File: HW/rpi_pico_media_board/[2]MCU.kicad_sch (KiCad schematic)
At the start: 1 part

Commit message: Scheme improvements
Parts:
- added D200: PMEG1030EJ,115, Diode_SMD:D_SOD-323F, symbol Device:D_Schottky
- added D201, D202, D203, D204, D205, D206: PESD3V3L1BA,115, Diode_SMD:D_SOD-323, symbol Device:D_TVS
- added J200, J201: Conn_01x04_Pin, Connector_PinSocket_2.54mm:PinSocket_1x04_P2.54mm_Vertical, symbol Connector:Conn_01x04_Pin
- added SW200: SW_DPDT_XLX, rpi_pico_media_board:SW_DPDT_XLX, symbol rpi_pico_media_board:SW_DPDT_XLX
- added U202, U203: mems-mic, rpi_pico_media_board:inmp441, symbol rpi_pico_media_board:mems-mic
- renumbered A1 to U200
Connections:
- net UART0_TX: now reaches U200.1 (GPIO0)
- net UART0_TX: now also D203.1 (A1), J200.2 (Pin_2)
- net PCF8563_INT: now reaches U200.10 (GPIO7)
- net SPI1_SD_CARD_MISO: now reaches U200.11 (GPIO8)
- net SPI1_SD_CARD_CS: now reaches U200.12 (GPIO9)
- net GND: now reaches U200.13 (GND), U200.18 (GND), U200.23 (GND), U200.28 (GND), U200.3 (GND), U200.38 (GND), U200.8 (GND)
- net GND: now also D201.2 (A2), D202.2 (A2), D203.2 (A2), D204.2 (A2), D205.2 (A2), D206.2 (A2), J200.1 (Pin_1), J201.1 (Pin_1), U202.2 (GND), U203.2 (GND), U203.6 (SEL)
- net SPI1_SD_CARD_SCK: now reaches U200.14 (GPIO10)
- net SPI1_SD_CARD_MOSI: now reaches U200.15 (GPIO11)
- net SPI1_SD_CARD_CARD_DETECT: now reaches U200.16 (GPIO12)
- net I2S_INMP441_DATA: now reaches U200.17 (GPIO13)
- net I2S_INMP441_DATA: now also U202.4 (DOUT), U203.4 (DOUT)
- net I2S_INMP441_SCK: now reaches U200.19 (GPIO14)
- net I2S_INMP441_SCK: now also U202.3 (BCLK), U203.3 (BCLK)
- net UART0_RX: now reaches U200.2 (GPIO1)
- net UART0_RX: now also D202.1 (A1), J200.3 (Pin_3)
- net I2S_INMP441_SCL: now reaches U200.20 (GPIO15)
- net I2S_INMP441_SCL: now also U202.5 (LRCLK), U203.5 (LRCLK)
- net MACRO_PAD_BTN_COL_0: now reaches U200.21 (GPIO16)
- net MACRO_PAD_BTN_COL_1: now reaches U200.22 (GPIO17)
- net MACRO_PAD_BTN_COL_2: now reaches U200.24 (GPIO18)
- net MACRO_PAD_BTN_COL_3: now reaches U200.25 (GPIO19)
- net MACRO_PAD_BTN_ROW_0: now reaches U200.26 (GPIO20)
- net MACRO_PAD_BTN_ROW_1: now reaches U200.27 (GPIO21)
- net MACRO_PAD_BTN_ROW_2: now reaches U200.29 (GPIO22)
- net USR_LED_0: now reaches U200.31 (GPIO26_ADC0)
- net USR_LED_1: now reaches U200.32 (GPIO27_ADC1)
- net USR_LED_2: now reaches U200.34 (GPIO28_ADC2)
- net I2C1_SDA: now reaches U200.4 (GPIO2)
- net I2C1_SDA: now also D206.1 (A1), J201.2 (Pin_2)
- net +RPI_VBUS: now reaches U200.40 (VBUS)
- net +RPI_VBUS: now also SW200.2, SW200.5
- net I2C1_SCL: now reaches U200.5 (GPIO3)
- net I2C1_SCL: now also D205.1 (A1), J201.3 (Pin_3)
- net I2S_PCM5102_DATA: now reaches U200.6 (GPIO4)
- net I2S_PCM5102_SCK: now reaches U200.7 (GPIO5)
- net I2S_PCM5102_SCL: now reaches U200.9 (GPIO6)
- new net: D200.2 (A), SW200.3, SW200.4
- new net +3.3V: D201.1 (A1), D204.1 (A1), J200.4 (Pin_4), J201.4 (Pin_4)
- new net +3.3VA: U202.1 (3V), U202.6 (SEL), U203.1 (3V)
- new net VCC: D200.1 (K)
- no-connect marks 0 -> 8
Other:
- note added: "I2C1 PIN header"
- note added: "INM441 Microphone"
- note added: "UART PIN header"
- note added: "[2]MCU"
- moved on the sheet: U200

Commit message: Minor BOM updates
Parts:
- D200: Manufacturer (none) -> Nexperia; Manufacturer Part Number (none) -> PMEG1030EJ,115; Manufacturer_Name Nexperia -> (none); Manufacturer_Part_Number PMEG1030EJ,115 -> (none)
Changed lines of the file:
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@@
 			)
 		)
-		(property "Manufacturer_Name" "Nexperia"
+		(property "Manufacturer_Name" ""
 			(at 201.93 31.75 0)
 			(effects
@@
 			)
 		)
-		(property "Manufacturer_Part_Number" "PMEG1030EJ,115"
+		(property "Manufacturer_Part_Number" ""
 			(at 201.93 31.75 0)
 			(effects
+				(font
+					(size 1.27 1.27)
+				)
+				(hide yes)
+			)
+		)
+		(property "Manufacturer" "Nexperia"
+			(at 201.93 31.75 0)
+			(effects
+				(font
+					(size 1.27 1.27)
+				)
+				(hide yes)
+			)
+		)
+		(property "Manufacturer Part Number" "PMEG1030EJ,115"
+			(at 201.93 31.75 0)
+			(effects

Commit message: DRC cleanup
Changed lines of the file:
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@@
 	)
 	(global_label "I2S_INMP441_DATA"
-		(shape input)
+		(shape output)
 		(at 125.73 105.41 180)
 		(fields_autoplaced yes)
@@
 	)
 	(global_label "I2S_INMP441_DATA"
-		(shape input)
+		(shape output)
 		(at 80.01 149.86 0)
 		(fields_autoplaced yes)
@@
 		)
 	)
-	(global_label "I2S_INMP441_DATA"
-		(shape input)
-		(at 78.74 179.07 0)
-		(fields_autoplaced yes)
-		(effects
-			(font
-				(size 1.27 1.27)
-			)
-			(justify left)
-		)
-		(property "Intersheetrefs" "${INTERSHEET_REFS}"
-			(at 99.3842 179.07 0)
-			(effects
-				(font
-					(size 1.27 1.27)
-				)
-				(justify left)
-				(hide yes)
-			)
-		)
-	)
 	(global_label "MACRO_PAD_BTN_COL_2"
 		(shape input)
@@
 			(effects
 				(font
+					(size 1.27 1.27)
+				)
+				(justify left)
+				(hide yes)
+			)
+		)
+	)
+	(global_label "I2S_INMP441_DATA"
+		(shape output)
+		(at 78.74 179.07 0)
+		(fields_autoplaced yes)
+		(effects
+			(font
+				(size 1.27 1.27)
+			)
+			(justify left)
+		)
+		(property "Intersheetrefs" "${INTERSHEET_REFS}"
+			(at 99.3842 179.07 0)
+			(effects
+				(font

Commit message: PCB initial placement
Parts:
- U200: footprint Module_RaspberryPi_Pico:RaspberryPi_Pico_Common -> Module_RaspberryPi_Pico:RaspberryPi_Pico_Common_THT
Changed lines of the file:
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@@
 			)
 		)
-		(property "Footprint" "Module_RaspberryPi_Pico:RaspberryPi_Pico_Common"
+		(property "Footprint" "Module_RaspberryPi_Pico:RaspberryPi_Pico_Common_THT"
 			(at 153.67 144.78 0)
 			(effects

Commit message: Very initial PCB layout
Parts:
- removed D204: PESD3V3L1BA,115, Diode_SMD:D_SOD-323, symbol Device:D_TVS
- removed J201: Conn_01x04_Pin, Connector_PinSocket_2.54mm:PinSocket_1x04_P2.54mm_Vertical, symbol Connector:Conn_01x04_Pin
- added J201: Conn_01x03, Connector_PinSocket_2.54mm:PinSocket_1x03_P2.54mm_Vertical, symbol Connector_Generic:Conn_01x03
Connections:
- net GND: now also J201.1 (Pin_1)
- net I2C1_SCL: now also J201.3 (Pin_3)
- net I2C1_SDA: now also J201.2 (Pin_2)
- net +3.3VA renamed +3.3VA_INMP

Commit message: Macro Pad routing
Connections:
- net MACRO_PAD_BTN_ROW_0: now also U200.29 (GPIO22); no longer U200.26 (GPIO20)
- net MACRO_PAD_BTN_ROW_2: now also U200.26 (GPIO20); no longer U200.29 (GPIO22)
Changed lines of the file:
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@@
+	(wire
+		(pts
+			(xy 176.53 92.71) (xy 182.88 92.71)
+		)
+		(stroke
+			(width 0)
+			(type default)
+		)
+	)
 	(wire
 		(pts
@@
 	(wire
 		(pts
+			(xy 176.53 90.17) (xy 182.88 90.17)
+		)
+		(stroke
+			(width 0)
+			(type default)
+		)
+	)
+	(wire
+		(pts
 			(xy 125.73 82.55) (xy 130.81 82.55)
 		)
@@
 	(wire
 		(pts
+			(xy 176.53 95.25) (xy 182.88 95.25)
+		)
+		(stroke
+			(width 0)
+			(type default)
+		)
+	)
+	(wire
+		(pts
 			(xy 250.19 135.89) (xy 242.57 135.89)
 		)
@@
 	(wire
 		(pts
-			(xy 176.53 90.17) (xy 182.88 90.17)
-		)
-		(stroke
-			(width 0)
-			(type default)
-		)
-	)
-	(wire
-		(pts
 			(xy 176.53 105.41) (xy 182.88 105.41)
 		)
@@
 	(wire
 		(pts
-			(xy 176.53 95.25) (xy 182.88 95.25)
-		)
-		(stroke
-			(width 0)
-			(type default)
-		)
-	)
-	(wire
-		(pts
 			(xy 26.67 140.97) (xy 26.67 154.94)
 		)
@@
 		(pts
 			(xy 176.53 107.95) (xy 182.88 107.95)
-		)
-		(stroke
-			(width 0)
-			(type default)
-		)
-	)
-	(wire
-		(pts
-			(xy 176.53 92.71) (xy 182.88 92.71)
 		)
 		(stroke
@@
 	(global_label "MACRO_PAD_BTN_ROW_0"
 		(shape input)
+		(at 182.88 95.25 0)
+		(fields_autoplaced yes)
+		(effects
+			(font
+				(size 1.27 1.27)
+			)
+			(justify left)
+		)
+		(property "Intersheetrefs" "${INTERSHEET_REFS}"
+			(at 208.6042 95.25 0)
+			(effects
+				(font
+					(size 1.27 1.27)
+				)
+				(justify left)
+				(hide yes)
+			)
+		)
+	)
+	(global_label "MACRO_PAD_BTN_ROW_2"
+		(shape input)
 		(at 182.88 90.17 0)
 		(fields_autoplaced yes)
@@
 			(effects
 				(font
-					(size 1.27 1.27)
-				)
-				(justify left)
-				(hide yes)
-			)
-		)
-	)
-	(global_label "MACRO_PAD_BTN_ROW_2"
-		(shape input)
-		(at 182.88 95.25 0)
-		(fields_autoplaced yes)
-		(effects
-			(font
-				(size 1.27 1.27)
-			)
-			(justify left)
-		)
-		(property "Intersheetrefs" "${INTERSHEET_REFS}"
-			(at 208.6042 95.25 0)
-			(effects
-				(font

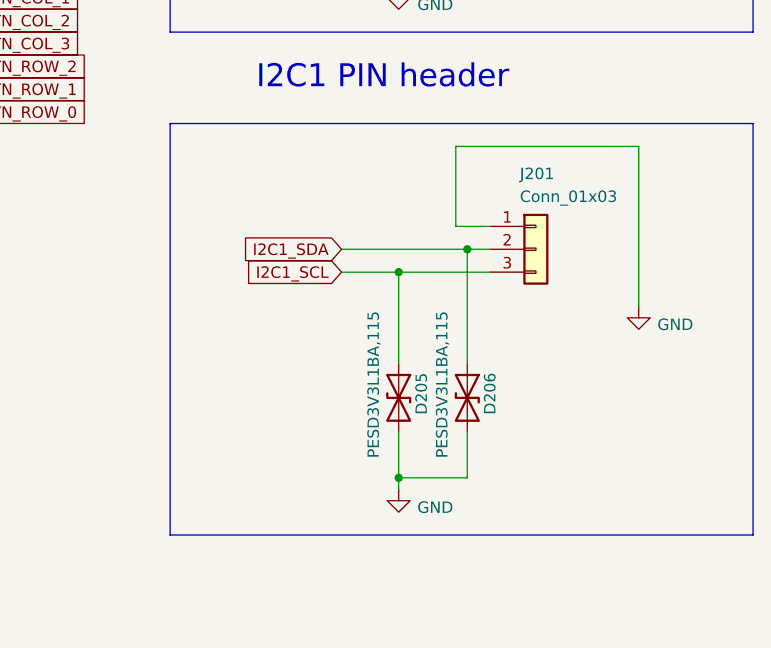
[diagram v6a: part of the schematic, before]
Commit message: SD Card routing
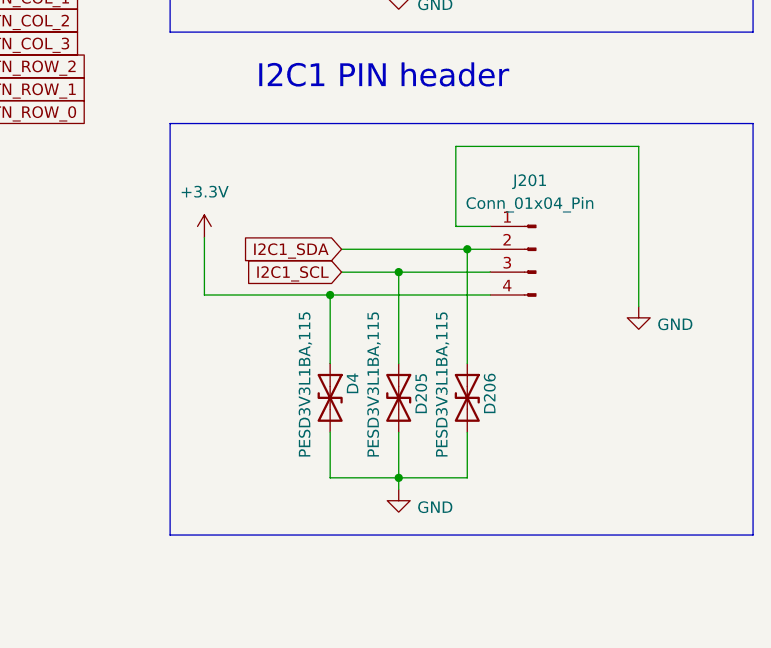
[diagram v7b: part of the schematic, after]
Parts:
- removed J201: Conn_01x03, Connector_PinSocket_2.54mm:PinSocket_1x03_P2.54mm_Vertical, symbol Connector_Generic:Conn_01x03
- added D4: PESD3V3L1BA,115, Diode_SMD:D_SOD-323, symbol Device:D_TVS
- added J201: Conn_01x04_Pin, Connector_PinHeader_2.54mm:PinHeader_1x04_P2.54mm_Vertical, symbol Connector:Conn_01x04_Pin
- J200: footprint Connector_PinSocket_2.54mm:PinSocket_1x04_P2.54mm_Vertical -> Connector_PinHeader_2.54mm:PinHeader_1x04_P2.54mm_Vertical
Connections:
- net +3.3V: now also D4.1 (A1), J201.4 (Pin_4)
- net GND: now also D4.2 (A2), J201.1 (Pin_1)
- net I2C1_SCL: now also J201.3 (Pin_3)
- net I2C1_SDA: now also J201.2 (Pin_2)
